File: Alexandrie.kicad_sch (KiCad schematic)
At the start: 47 parts, among them J1 kk_10, J11 CONN_01X03, J2 kk_5, J3 kk_5, J4 CONN_01X06, J5 CONN_01X02, J6 CONN_01X13, J7 Conn_01x07, J8 kk_10, U1 74HCT04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

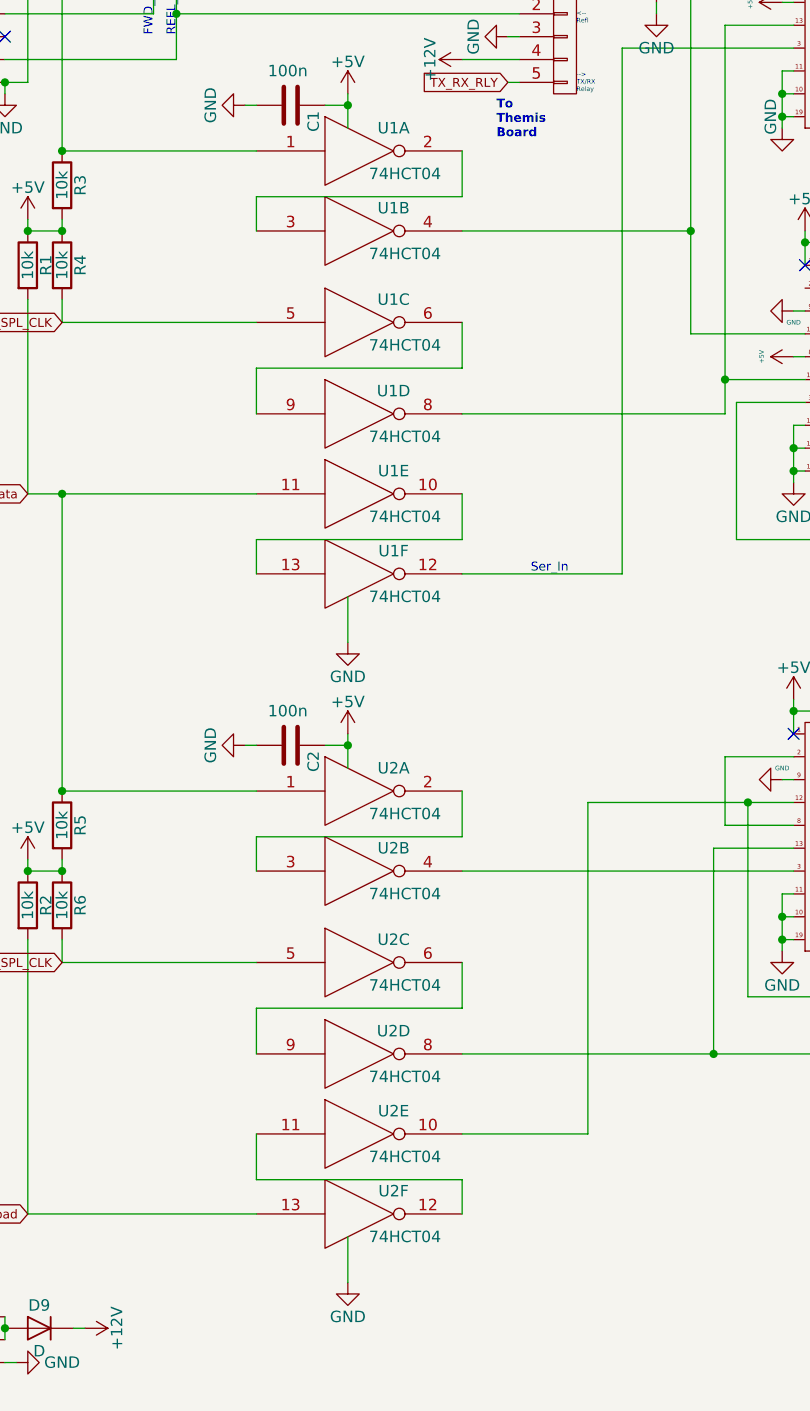
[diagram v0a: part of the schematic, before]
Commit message: kicad 10 update, new readme, new Wiki
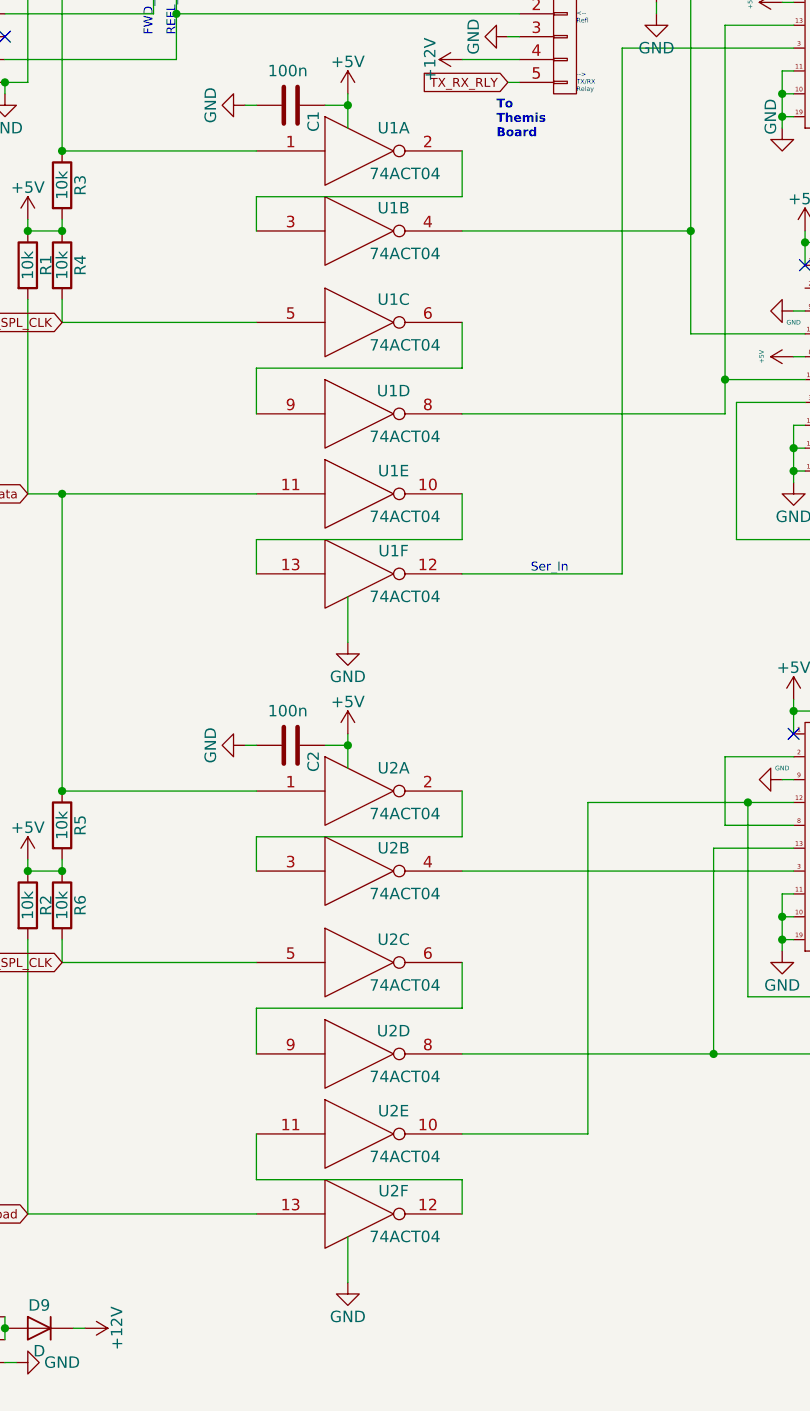
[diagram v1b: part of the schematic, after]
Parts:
- U1, U2: value 74HCT04 -> 74ACT04
